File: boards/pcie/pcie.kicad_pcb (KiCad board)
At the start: 4 copper layers, 167.7 x 111.2 mm, 136 parts, among them J1 PCIexpress_bracket, J10 HDMI_A, J11 HDMI_A, J2 PCIexpress_x16, J3 12V, J4 5V, J5 3V3, J6 1V0, J7 GND, J8 HDMI_A, J9 HDMI_A, U1 AP63203WU, U2 UPD720202K8-701-BAA, U3 AP63205WU, U4 TLV75801PDBVR, U5 CH334F, U6 CH334F, U7 CH334F, U8 CH334F

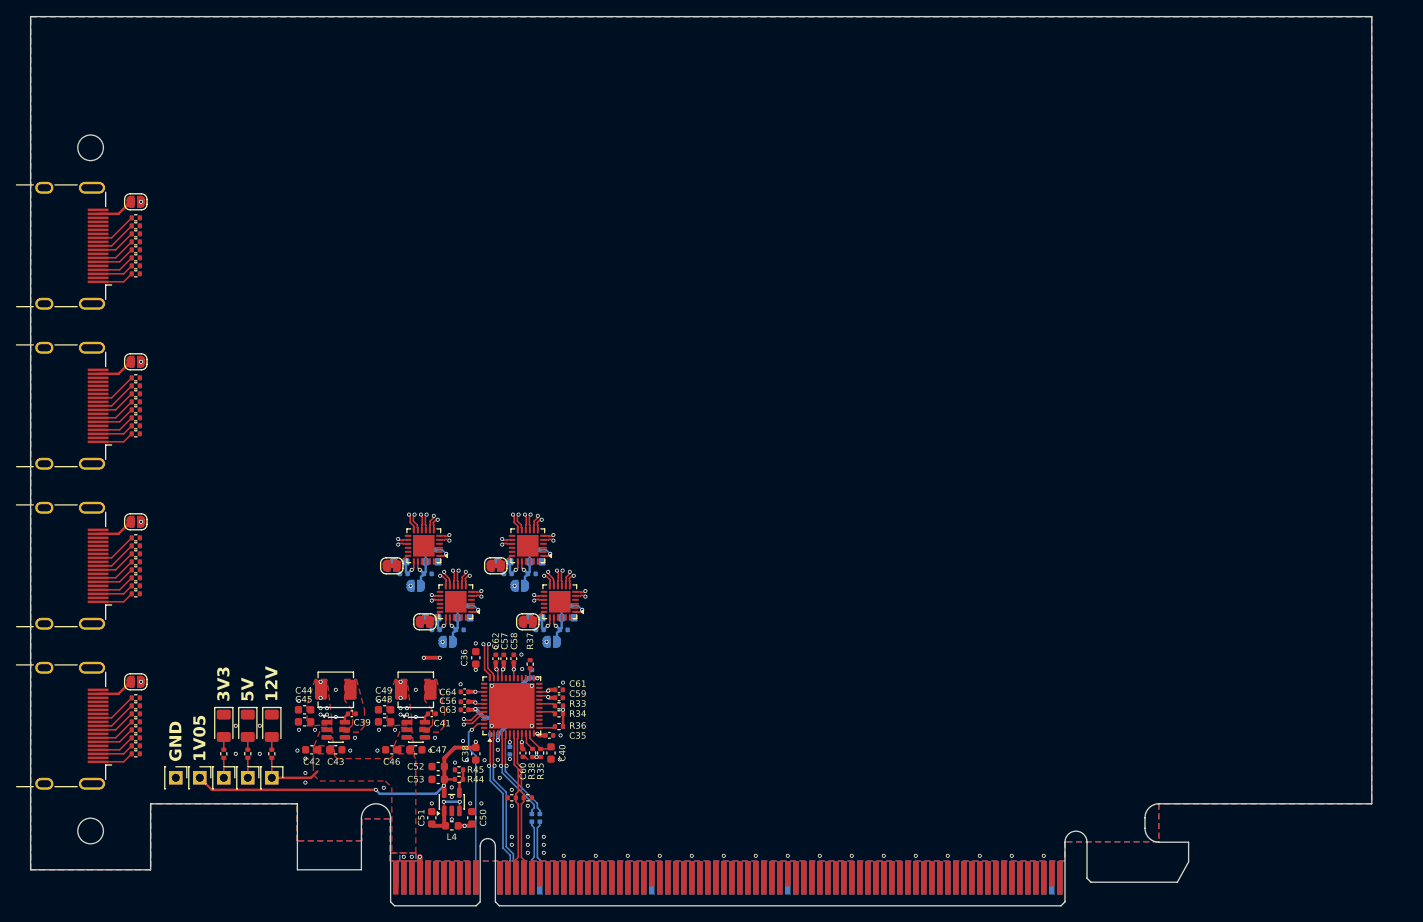
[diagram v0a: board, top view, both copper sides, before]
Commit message: pcie: add leds, buck regulators
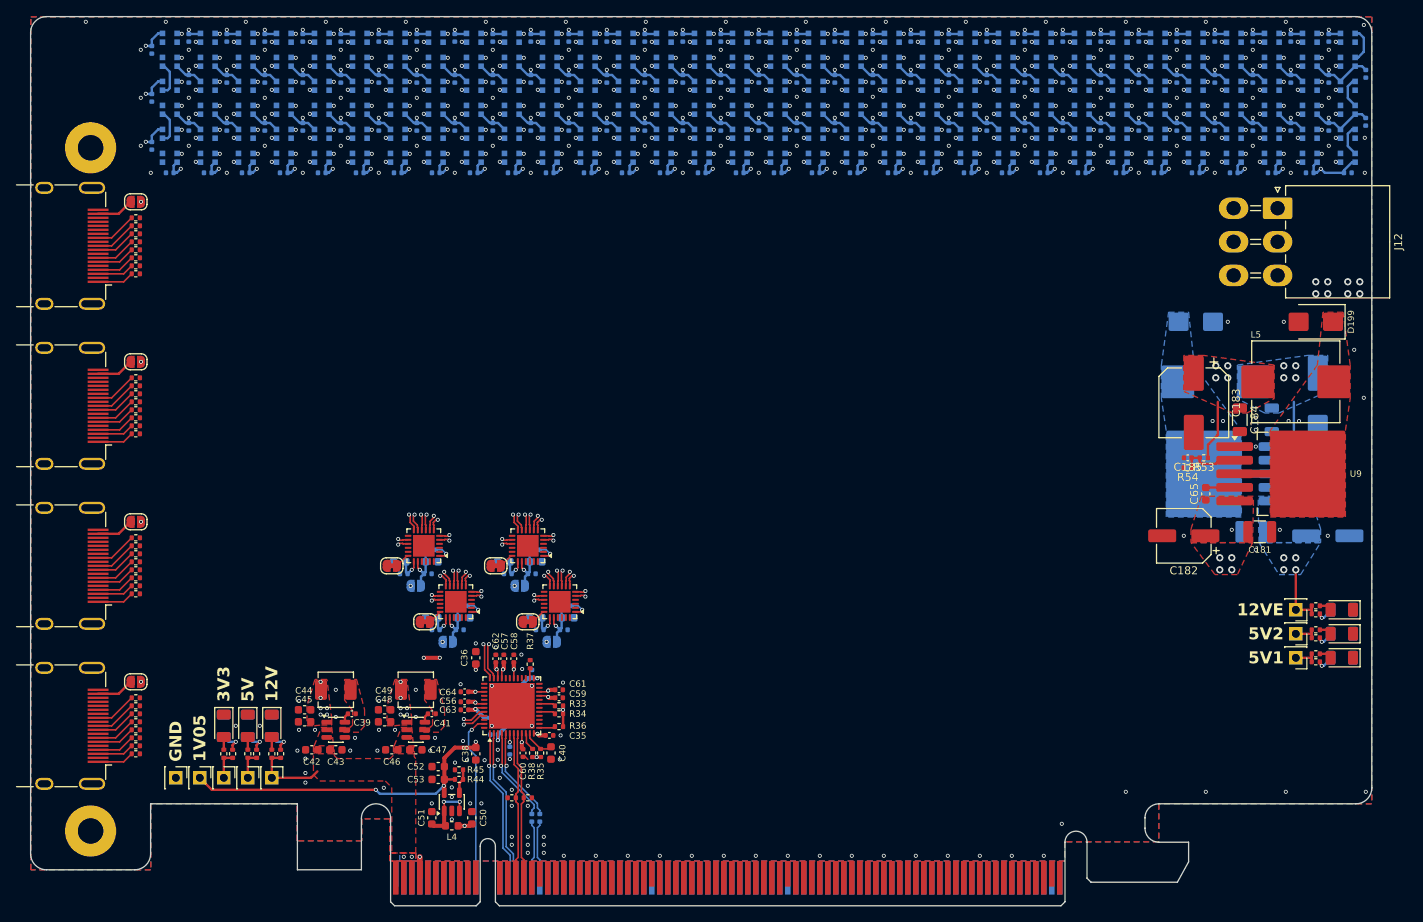
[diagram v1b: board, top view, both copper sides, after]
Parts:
- added C100: 100nF, Capacitor_SMD:C_0402_1005Metric, B.Cu at (165.0, 96.8)
- added C101: 100nF, Capacitor_SMD:C_0402_1005Metric, B.Cu at (174.5, 96.8)
- added C102: 100nF, Capacitor_SMD:C_0402_1005Metric, B.Cu at (169.8, 96.8)
- added C103: 100nF, Capacitor_SMD:C_0402_1005Metric, B.Cu at (179.2, 96.8)
- added C104: 100nF, Capacitor_SMD:C_0402_1005Metric, B.Cu at (207.8, 96.8)
- added C105: 100nF, Capacitor_SMD:C_0402_1005Metric, B.Cu at (203.0, 96.8)
- added C106: 100nF, Capacitor_SMD:C_0402_1005Metric, B.Cu at (198.2, 96.8)
- added C107: 100nF, Capacitor_SMD:C_0402_1005Metric, B.Cu at (193.5, 96.8)
- added C108: 100nF, Capacitor_SMD:C_0402_1005Metric, B.Cu at (184.0, 96.8)
- added C109: 100nF, Capacitor_SMD:C_0402_1005Metric, B.Cu at (188.8, 96.8)
- added C110: 100nF, Capacitor_SMD:C_0402_1005Metric, B.Cu at (136.5, 96.8)
- added C111: 100nF, Capacitor_SMD:C_0402_1005Metric, B.Cu at (141.2, 96.8)
- added C112: 100nF, Capacitor_SMD:C_0402_1005Metric, B.Cu at (224.4, 102.5)
- added C113: 100nF, Capacitor_SMD:C_0402_1005Metric, B.Cu at (212.5, 96.8)
- added C114: 100nF, Capacitor_SMD:C_0402_1005Metric, B.Cu at (217.2, 96.8)
- added C115: 100nF, Capacitor_SMD:C_0402_1005Metric, B.Cu at (222.0, 96.8)
- added C116: 100nF, Capacitor_SMD:C_0402_1005Metric, B.Cu at (226.8, 96.8)
- added C117: 100nF, Capacitor_SMD:C_0402_1005Metric, B.Cu at (96.1, 102.5)
- added C118: 100nF, Capacitor_SMD:C_0402_1005Metric, B.Cu at (134.1, 102.5)
- added C119: 100nF, Capacitor_SMD:C_0402_1005Metric, B.Cu at (153.1, 102.5)
- added C120: 100nF, Capacitor_SMD:C_0402_1005Metric, B.Cu at (115.1, 102.5)
- added C121: 100nF, Capacitor_SMD:C_0402_1005Metric, B.Cu at (172.1, 102.5)
- added C122: 100nF, Capacitor_SMD:C_0402_1005Metric, B.Cu at (219.6, 102.5)
- added C123: 100nF, Capacitor_SMD:C_0402_1005Metric, B.Cu at (200.6, 102.5)
- added C124: 100nF, Capacitor_SMD:C_0402_1005Metric, B.Cu at (191.1, 102.5)
- added C125: 100nF, Capacitor_SMD:C_0402_1005Metric, B.Cu at (91.4, 102.5)
- added C126: 100nF, Capacitor_SMD:C_0402_1005Metric, B.Cu at (129.4, 102.5)
- added C127: 100nF, Capacitor_SMD:C_0402_1005Metric, B.Cu at (148.4, 102.5)
- added C128: 100nF, Capacitor_SMD:C_0402_1005Metric, B.Cu at (110.4, 102.5)
- added C129: 100nF, Capacitor_SMD:C_0402_1005Metric, B.Cu at (167.4, 102.5)
- added C130: 100nF, Capacitor_SMD:C_0402_1005Metric, B.Cu at (214.9, 102.5)
- added C131: 100nF, Capacitor_SMD:C_0402_1005Metric, B.Cu at (195.9, 102.5)
- added C132: 100nF, Capacitor_SMD:C_0402_1005Metric, B.Cu at (229.1, 102.5)
- added C133: 100nF, Capacitor_SMD:C_0402_1005Metric, B.Cu at (86.6, 102.5)
- added C134: 100nF, Capacitor_SMD:C_0402_1005Metric, B.Cu at (124.6, 102.5)
- added C135: 100nF, Capacitor_SMD:C_0402_1005Metric, B.Cu at (143.6, 102.5)
- added C136: 100nF, Capacitor_SMD:C_0402_1005Metric, B.Cu at (105.6, 102.5)
- added C137: 100nF, Capacitor_SMD:C_0402_1005Metric, B.Cu at (162.6, 102.5)
- added C138: 100nF, Capacitor_SMD:C_0402_1005Metric, B.Cu at (210.1, 102.5)
- added C139: 100nF, Capacitor_SMD:C_0402_1005Metric, B.Cu at (186.4, 102.5)
- added C140: 100nF, Capacitor_SMD:C_0402_1005Metric, B.Cu at (176.9, 102.5)
- added C141: 100nF, Capacitor_SMD:C_0402_1005Metric, B.Cu at (81.9, 102.5)
- added C142: 100nF, Capacitor_SMD:C_0402_1005Metric, B.Cu at (119.9, 102.5)
- added C143: 100nF, Capacitor_SMD:C_0402_1005Metric, B.Cu at (138.9, 102.5)
- added C144: 100nF, Capacitor_SMD:C_0402_1005Metric, B.Cu at (100.9, 102.5)
- added C145: 100nF, Capacitor_SMD:C_0402_1005Metric, B.Cu at (157.9, 102.5)
- added C146: 100nF, Capacitor_SMD:C_0402_1005Metric, B.Cu at (205.4, 102.5)
- added C147: 100nF, Capacitor_SMD:C_0402_1005Metric, B.Cu at (181.6, 102.5)
- added C148: 100nF, Capacitor_SMD:C_0402_1005Metric, B.Cu at (231.4, 96.1)
- added C149: 100nF, Capacitor_SMD:C_0402_1005Metric, B.Cu at (184.0, 85.6)
- added C150: 100nF, Capacitor_SMD:C_0402_1005Metric, B.Cu at (188.8, 85.6)
- added C151: 100nF, Capacitor_SMD:C_0402_1005Metric, B.Cu at (193.5, 85.6)
- added C152: 100nF, Capacitor_SMD:C_0402_1005Metric, B.Cu at (198.2, 85.6)
- added C153: 100nF, Capacitor_SMD:C_0402_1005Metric, B.Cu at (203.0, 85.6)
- added C154: 100nF, Capacitor_SMD:C_0402_1005Metric, B.Cu at (207.8, 85.6)
- added C155: 100nF, Capacitor_SMD:C_0402_1005Metric, B.Cu at (212.5, 85.6)
- added C156: 100nF, Capacitor_SMD:C_0402_1005Metric, B.Cu at (217.2, 85.6)
- added C157: 100nF, Capacitor_SMD:C_0402_1005Metric, B.Cu at (146.0, 85.6)
- added C158: 100nF, Capacitor_SMD:C_0402_1005Metric, B.Cu at (150.8, 85.6)
- added C159: 100nF, Capacitor_SMD:C_0402_1005Metric, B.Cu at (155.5, 85.6)
- added C160: 100nF, Capacitor_SMD:C_0402_1005Metric, B.Cu at (160.2, 85.6)
- added C161: 100nF, Capacitor_SMD:C_0402_1005Metric, B.Cu at (165.0, 85.6)
- added C162: 100nF, Capacitor_SMD:C_0402_1005Metric, B.Cu at (169.8, 85.6)
- added C163: 100nF, Capacitor_SMD:C_0402_1005Metric, B.Cu at (174.5, 85.6)
- added C164: 100nF, Capacitor_SMD:C_0402_1005Metric, B.Cu at (179.2, 85.6)
- added C165: 100nF, Capacitor_SMD:C_0402_1005Metric, B.Cu at (108.0, 85.6)
- added C166: 100nF, Capacitor_SMD:C_0402_1005Metric, B.Cu at (112.8, 85.6)
- added C167: 100nF, Capacitor_SMD:C_0402_1005Metric, B.Cu at (117.5, 85.6)
- added C168: 100nF, Capacitor_SMD:C_0402_1005Metric, B.Cu at (122.2, 85.6)
- added C169: 100nF, Capacitor_SMD:C_0402_1005Metric, B.Cu at (127.0, 85.6)
- added C170: 100nF, Capacitor_SMD:C_0402_1005Metric, B.Cu at (131.8, 85.6)
- added C171: 100nF, Capacitor_SMD:C_0402_1005Metric, B.Cu at (136.5, 85.6)
- added C172: 100nF, Capacitor_SMD:C_0402_1005Metric, B.Cu at (141.2, 85.6)
- added C173: 100nF, Capacitor_SMD:C_0402_1005Metric, B.Cu at (84.2, 85.6)
- added C174: 100nF, Capacitor_SMD:C_0402_1005Metric, B.Cu at (89.0, 85.6)
- added C175: 100nF, Capacitor_SMD:C_0402_1005Metric, B.Cu at (93.8, 85.6)
- added C176: 100nF, Capacitor_SMD:C_0402_1005Metric, B.Cu at (98.5, 85.6)
- added C177: 100nF, Capacitor_SMD:C_0402_1005Metric, B.Cu at (103.2, 85.6)
- added C178: 100nF, Capacitor_SMD:C_0402_1005Metric, B.Cu at (231.4, 90.1)
- added C179: 100nF, Capacitor_SMD:C_0402_1005Metric, B.Cu at (226.8, 85.6)
- added C180: 100nF, Capacitor_SMD:C_0402_1005Metric, B.Cu at (222.0, 85.6)
- added C181: 22uF@25V, Capacitor_SMD:C_1210_3225Metric, F.Cu at (218.1, 147.4)
- added C182: 220uF@25V, Capacitor_SMD:CP_Elec_6.3x7.7, F.Cu at (208.6, 147.9)
- added C183: 470uF@16V, Capacitor_SMD:CP_Elec_8x10.5, F.Cu at (209.9, 131.2)
- added C184: 22uF@10V, Capacitor_SMD:C_1206_3216Metric, F.Cu at (215.6, 133.4)
- added C185: 33nF, Capacitor_SMD:C_0402_1005Metric, F.Cu at (209.1, 138.1)
- added C186: 220uF@25V, Capacitor_SMD:CP_Elec_6.3x7.7, B.Cu at (226.6, 147.9)
- added C187: 22uF@25V, Capacitor_SMD:C_1210_3225Metric, B.Cu at (217.1, 147.4)
- added C188: 1uF, Capacitor_SMD:C_0603_1608Metric, B.Cu at (223.9, 142.6)
- added C189: 33nF, Capacitor_SMD:C_0402_1005Metric, B.Cu at (226.1, 138.1)
- added C19: 100nF, Capacitor_SMD:C_0402_1005Metric, B.Cu at (79.6, 87.1)
- added C190: 22uF@10V, Capacitor_SMD:C_1206_3216Metric, B.Cu at (219.6, 133.4)
- added C191: 470uF@16V, Capacitor_SMD:CP_Elec_8x10.5, B.Cu at (225.4, 131.2)
- added C20: 100nF, Capacitor_SMD:C_0402_1005Metric, B.Cu at (79.6, 93.1)
- added C21: 100nF, Capacitor_SMD:C_0402_1005Metric, B.Cu at (89.0, 90.8)
- added C22: 100nF, Capacitor_SMD:C_0402_1005Metric, B.Cu at (84.2, 90.8)
- added C23: 100nF, Capacitor_SMD:C_0402_1005Metric, B.Cu at (93.8, 96.8)
- added C24: 100nF, Capacitor_SMD:C_0402_1005Metric, B.Cu at (89.0, 96.8)
- added C25: 100nF, Capacitor_SMD:C_0402_1005Metric, B.Cu at (84.2, 96.8)
- added C26: 100nF, Capacitor_SMD:C_0402_1005Metric, B.Cu at (79.6, 99.1)
- added C27: 100nF, Capacitor_SMD:C_0402_1005Metric, B.Cu at (93.8, 90.8)
- added C28: 100nF, Capacitor_SMD:C_0402_1005Metric, B.Cu at (98.5, 90.8)
- added C29: 100nF, Capacitor_SMD:C_0402_1005Metric, B.Cu at (103.2, 90.8)
- added C30: 100nF, Capacitor_SMD:C_0402_1005Metric, B.Cu at (108.0, 90.8)
- added C31: 100nF, Capacitor_SMD:C_0402_1005Metric, B.Cu at (112.8, 90.8)
- added C32: 100nF, Capacitor_SMD:C_0402_1005Metric, B.Cu at (117.5, 90.8)
- added C37: 100nF, Capacitor_SMD:C_0402_1005Metric, B.Cu at (122.2, 90.8)
- added C65: 1uF, Capacitor_SMD:C_0603_1608Metric, F.Cu at (211.4, 142.6)
- added C66: 100nF, Capacitor_SMD:C_0402_1005Metric, B.Cu at (127.0, 90.8)
- added C67: 100nF, Capacitor_SMD:C_0402_1005Metric, B.Cu at (131.8, 90.8)
- added C68: 100nF, Capacitor_SMD:C_0402_1005Metric, B.Cu at (174.5, 90.8)
- added C69: 100nF, Capacitor_SMD:C_0402_1005Metric, B.Cu at (179.2, 90.8)
- added C70: 100nF, Capacitor_SMD:C_0402_1005Metric, B.Cu at (184.0, 90.8)
- added C71: 100nF, Capacitor_SMD:C_0402_1005Metric, B.Cu at (188.8, 90.8)
- added C72: 100nF, Capacitor_SMD:C_0402_1005Metric, B.Cu at (155.5, 90.8)
- added C73: 100nF, Capacitor_SMD:C_0402_1005Metric, B.Cu at (160.2, 90.8)
- added C74: 100nF, Capacitor_SMD:C_0402_1005Metric, B.Cu at (165.0, 90.8)
- added C75: 100nF, Capacitor_SMD:C_0402_1005Metric, B.Cu at (169.8, 90.8)
- added C76: 100nF, Capacitor_SMD:C_0402_1005Metric, B.Cu at (141.2, 90.8)
- added C77: 100nF, Capacitor_SMD:C_0402_1005Metric, B.Cu at (136.5, 90.8)
- added C78: 100nF, Capacitor_SMD:C_0402_1005Metric, B.Cu at (150.8, 90.8)
- added C79: 100nF, Capacitor_SMD:C_0402_1005Metric, B.Cu at (146.0, 90.8)
- added C80: 100nF, Capacitor_SMD:C_0402_1005Metric, B.Cu at (193.5, 90.8)
- added C81: 100nF, Capacitor_SMD:C_0402_1005Metric, B.Cu at (198.2, 90.8)
- added C82: 100nF, Capacitor_SMD:C_0402_1005Metric, B.Cu at (203.0, 90.8)
- added C83: 100nF, Capacitor_SMD:C_0402_1005Metric, B.Cu at (207.8, 90.8)
- added C84: 100nF, Capacitor_SMD:C_0402_1005Metric, B.Cu at (226.8, 90.8)
- added C85: 100nF, Capacitor_SMD:C_0402_1005Metric, B.Cu at (212.5, 90.8)
- added C86: 100nF, Capacitor_SMD:C_0402_1005Metric, B.Cu at (217.2, 90.8)
- added C87: 100nF, Capacitor_SMD:C_0402_1005Metric, B.Cu at (222.0, 90.8)
- added C88: 100nF, Capacitor_SMD:C_0402_1005Metric, B.Cu at (98.5, 96.8)
- added C89: 100nF, Capacitor_SMD:C_0402_1005Metric, B.Cu at (103.2, 96.8)
- added C90: 100nF, Capacitor_SMD:C_0402_1005Metric, B.Cu at (112.8, 96.8)
- added C91: 100nF, Capacitor_SMD:C_0402_1005Metric, B.Cu at (108.0, 96.8)
- added C92: 100nF, Capacitor_SMD:C_0402_1005Metric, B.Cu at (117.5, 96.8)
- added C93: 100nF, Capacitor_SMD:C_0402_1005Metric, B.Cu at (122.2, 96.8)
- added C94: 100nF, Capacitor_SMD:C_0402_1005Metric, B.Cu at (127.0, 96.8)
- added C95: 100nF, Capacitor_SMD:C_0402_1005Metric, B.Cu at (131.8, 96.8)
- added C96: 100nF, Capacitor_SMD:C_0402_1005Metric, B.Cu at (150.8, 96.8)
- added C97: 100nF, Capacitor_SMD:C_0402_1005Metric, B.Cu at (155.5, 96.8)
- added C98: 100nF, Capacitor_SMD:C_0402_1005Metric, B.Cu at (146.0, 96.8)
- added C99: 100nF, Capacitor_SMD:C_0402_1005Metric, B.Cu at (160.2, 96.8)
- added D10: LED_45deg, pcie:LED_WS2812B-2020_PLCC4_2.0x2.0mm, B.Cu at (96.1, 85.6)
- added D100: LED_45deg, pcie:LED_WS2812B-2020_PLCC4_2.0x2.0mm, B.Cu at (219.6, 91.6)
- added D101: LED_45deg, pcie:LED_WS2812B-2020_PLCC4_2.0x2.0mm, B.Cu at (224.4, 91.6)
- added D102: LED_45deg, pcie:LED_WS2812B-2020_PLCC4_2.0x2.0mm, B.Cu at (229.1, 91.6)
- added D103: LED_45deg, pcie:LED_WS2812B-2020_PLCC4_2.0x2.0mm, B.Cu at (229.1, 94.6)
- added D104: LED_45deg, pcie:LED_WS2812B-2020_PLCC4_2.0x2.0mm, B.Cu at (224.4, 94.6)
- added D105: LED_45deg, pcie:LED_WS2812B-2020_PLCC4_2.0x2.0mm, B.Cu at (219.6, 94.6)
- added D106: LED_45deg, pcie:LED_WS2812B-2020_PLCC4_2.0x2.0mm, B.Cu at (214.9, 94.6)
- added D107: LED_45deg, pcie:LED_WS2812B-2020_PLCC4_2.0x2.0mm, B.Cu at (210.1, 94.6)
- added D108: LED_45deg, pcie:LED_WS2812B-2020_PLCC4_2.0x2.0mm, B.Cu at (205.4, 94.6)
- added D109: LED_45deg, pcie:LED_WS2812B-2020_PLCC4_2.0x2.0mm, B.Cu at (200.6, 94.6)
- added D11: LED_45deg, pcie:LED_WS2812B-2020_PLCC4_2.0x2.0mm, B.Cu at (100.9, 85.6)
- added D110: LED_45deg, pcie:LED_WS2812B-2020_PLCC4_2.0x2.0mm, B.Cu at (195.9, 94.6)
- added D111: LED_45deg, pcie:LED_WS2812B-2020_PLCC4_2.0x2.0mm, B.Cu at (191.1, 94.6)
- added D112: LED_45deg, pcie:LED_WS2812B-2020_PLCC4_2.0x2.0mm, B.Cu at (186.4, 94.6)
- added D113: LED_45deg, pcie:LED_WS2812B-2020_PLCC4_2.0x2.0mm, B.Cu at (181.6, 94.6)
- added D114: LED_45deg, pcie:LED_WS2812B-2020_PLCC4_2.0x2.0mm, B.Cu at (176.9, 94.6)
- added D115: LED_45deg, pcie:LED_WS2812B-2020_PLCC4_2.0x2.0mm, B.Cu at (172.1, 94.6)
- added D116: LED_45deg, pcie:LED_WS2812B-2020_PLCC4_2.0x2.0mm, B.Cu at (167.4, 94.6)
- added D117: LED_45deg, pcie:LED_WS2812B-2020_PLCC4_2.0x2.0mm, B.Cu at (162.6, 94.6)
- added D118: LED_45deg, pcie:LED_WS2812B-2020_PLCC4_2.0x2.0mm, B.Cu at (157.9, 94.6)
- added D119: LED_45deg, pcie:LED_WS2812B-2020_PLCC4_2.0x2.0mm, B.Cu at (153.1, 94.6)
- added D12: LED_45deg, pcie:LED_WS2812B-2020_PLCC4_2.0x2.0mm, B.Cu at (105.6, 85.6)
- added D120: LED_45deg, pcie:LED_WS2812B-2020_PLCC4_2.0x2.0mm, B.Cu at (148.4, 94.6)
- added D121: LED_45deg, pcie:LED_WS2812B-2020_PLCC4_2.0x2.0mm, B.Cu at (143.6, 94.6)
- added D122: LED_45deg, pcie:LED_WS2812B-2020_PLCC4_2.0x2.0mm, B.Cu at (138.9, 94.6)
- added D123: LED_45deg, pcie:LED_WS2812B-2020_PLCC4_2.0x2.0mm, B.Cu at (134.1, 94.6)
- added D124: LED_45deg, pcie:LED_WS2812B-2020_PLCC4_2.0x2.0mm, B.Cu at (129.4, 94.6)
- added D125: LED_45deg, pcie:LED_WS2812B-2020_PLCC4_2.0x2.0mm, B.Cu at (124.6, 94.6)
- added D126: LED_45deg, pcie:LED_WS2812B-2020_PLCC4_2.0x2.0mm, B.Cu at (119.9, 94.6)
- added D127: LED_45deg, pcie:LED_WS2812B-2020_PLCC4_2.0x2.0mm, B.Cu at (115.1, 94.6)
- added D128: LED_45deg, pcie:LED_WS2812B-2020_PLCC4_2.0x2.0mm, B.Cu at (110.4, 94.6)
- added D129: LED_45deg, pcie:LED_WS2812B-2020_PLCC4_2.0x2.0mm, B.Cu at (105.6, 94.6)
- added D13: LED_45deg, pcie:LED_WS2812B-2020_PLCC4_2.0x2.0mm, B.Cu at (110.4, 85.6)
- added D130: LED_45deg, pcie:LED_WS2812B-2020_PLCC4_2.0x2.0mm, B.Cu at (100.9, 94.6)
- added D131: LED_45deg, pcie:LED_WS2812B-2020_PLCC4_2.0x2.0mm, B.Cu at (96.1, 94.6)
- added D132: LED_45deg, pcie:LED_WS2812B-2020_PLCC4_2.0x2.0mm, B.Cu at (91.4, 94.6)
- added D133: LED_45deg, pcie:LED_WS2812B-2020_PLCC4_2.0x2.0mm, B.Cu at (86.6, 94.6)
- added D134: LED_45deg, pcie:LED_WS2812B-2020_PLCC4_2.0x2.0mm, B.Cu at (81.9, 94.6)
- added D135: LED_45deg, pcie:LED_WS2812B-2020_PLCC4_2.0x2.0mm, B.Cu at (81.9, 97.6)
- added D136: LED_45deg, pcie:LED_WS2812B-2020_PLCC4_2.0x2.0mm, B.Cu at (86.6, 97.6)
- added D137: LED_45deg, pcie:LED_WS2812B-2020_PLCC4_2.0x2.0mm, B.Cu at (91.4, 97.6)
- added D138: LED_45deg, pcie:LED_WS2812B-2020_PLCC4_2.0x2.0mm, B.Cu at (96.1, 97.6)
- added D139: LED_45deg, pcie:LED_WS2812B-2020_PLCC4_2.0x2.0mm, B.Cu at (100.9, 97.6)
- added D14: LED_45deg, pcie:LED_WS2812B-2020_PLCC4_2.0x2.0mm, B.Cu at (115.1, 85.6)
- added D140: LED_45deg, pcie:LED_WS2812B-2020_PLCC4_2.0x2.0mm, B.Cu at (105.6, 97.6)
- added D141: LED_45deg, pcie:LED_WS2812B-2020_PLCC4_2.0x2.0mm, B.Cu at (110.4, 97.6)
- added D142: LED_45deg, pcie:LED_WS2812B-2020_PLCC4_2.0x2.0mm, B.Cu at (115.1, 97.6)
- added D143: LED_45deg, pcie:LED_WS2812B-2020_PLCC4_2.0x2.0mm, B.Cu at (119.9, 97.6)
- added D144: LED_45deg, pcie:LED_WS2812B-2020_PLCC4_2.0x2.0mm, B.Cu at (124.6, 97.6)
- added D145: LED_45deg, pcie:LED_WS2812B-2020_PLCC4_2.0x2.0mm, B.Cu at (129.4, 97.6)
- added D146: LED_45deg, pcie:LED_WS2812B-2020_PLCC4_2.0x2.0mm, B.Cu at (134.1, 97.6)
- added D147: LED_45deg, pcie:LED_WS2812B-2020_PLCC4_2.0x2.0mm, B.Cu at (138.9, 97.6)
- added D148: LED_45deg, pcie:LED_WS2812B-2020_PLCC4_2.0x2.0mm, B.Cu at (143.6, 97.6)
- added D149: LED_45deg, pcie:LED_WS2812B-2020_PLCC4_2.0x2.0mm, B.Cu at (148.4, 97.6)
- added D15: LED_45deg, pcie:LED_WS2812B-2020_PLCC4_2.0x2.0mm, B.Cu at (119.9, 85.6)
- added D150: LED_45deg, pcie:LED_WS2812B-2020_PLCC4_2.0x2.0mm, B.Cu at (153.1, 97.6)
- added D151: LED_45deg, pcie:LED_WS2812B-2020_PLCC4_2.0x2.0mm, B.Cu at (157.9, 97.6)
- added D152: LED_45deg, pcie:LED_WS2812B-2020_PLCC4_2.0x2.0mm, B.Cu at (162.6, 97.6)
- added D153: LED_45deg, pcie:LED_WS2812B-2020_PLCC4_2.0x2.0mm, B.Cu at (167.4, 97.6)
- added D154: LED_45deg, pcie:LED_WS2812B-2020_PLCC4_2.0x2.0mm, B.Cu at (172.1, 97.6)
- added D155: LED_45deg, pcie:LED_WS2812B-2020_PLCC4_2.0x2.0mm, B.Cu at (176.9, 97.6)
- added D156: LED_45deg, pcie:LED_WS2812B-2020_PLCC4_2.0x2.0mm, B.Cu at (181.6, 97.6)
- added D157: LED_45deg, pcie:LED_WS2812B-2020_PLCC4_2.0x2.0mm, B.Cu at (186.4, 97.6)
- added D158: LED_45deg, pcie:LED_WS2812B-2020_PLCC4_2.0x2.0mm, B.Cu at (191.1, 97.6)
- added D159: LED_45deg, pcie:LED_WS2812B-2020_PLCC4_2.0x2.0mm, B.Cu at (195.9, 97.6)
- added D16: LED_45deg, pcie:LED_WS2812B-2020_PLCC4_2.0x2.0mm, B.Cu at (124.6, 85.6)
- added D160: LED_45deg, pcie:LED_WS2812B-2020_PLCC4_2.0x2.0mm, B.Cu at (200.6, 97.6)
- added D161: LED_45deg, pcie:LED_WS2812B-2020_PLCC4_2.0x2.0mm, B.Cu at (205.4, 97.6)
- added D162: LED_45deg, pcie:LED_WS2812B-2020_PLCC4_2.0x2.0mm, B.Cu at (210.1, 97.6)
- added D163: LED_45deg, pcie:LED_WS2812B-2020_PLCC4_2.0x2.0mm, B.Cu at (214.9, 97.6)
- added D164: LED_45deg, pcie:LED_WS2812B-2020_PLCC4_2.0x2.0mm, B.Cu at (219.6, 97.6)
- added D165: LED_45deg, pcie:LED_WS2812B-2020_PLCC4_2.0x2.0mm, B.Cu at (224.4, 97.6)
- added D166: LED_45deg, pcie:LED_WS2812B-2020_PLCC4_2.0x2.0mm, B.Cu at (229.1, 97.6)
- added D167: LED_45deg, pcie:LED_WS2812B-2020_PLCC4_2.0x2.0mm, B.Cu at (229.1, 100.6)
- added D168: LED_45deg, pcie:LED_WS2812B-2020_PLCC4_2.0x2.0mm, B.Cu at (224.4, 100.6)
- added D169: LED_45deg, pcie:LED_WS2812B-2020_PLCC4_2.0x2.0mm, B.Cu at (219.6, 100.6)
- added D17: LED_45deg, pcie:LED_WS2812B-2020_PLCC4_2.0x2.0mm, B.Cu at (129.4, 85.6)
- added D170: LED_45deg, pcie:LED_WS2812B-2020_PLCC4_2.0x2.0mm, B.Cu at (214.9, 100.6)
- added D171: LED_45deg, pcie:LED_WS2812B-2020_PLCC4_2.0x2.0mm, B.Cu at (210.1, 100.6)
- added D172: LED_45deg, pcie:LED_WS2812B-2020_PLCC4_2.0x2.0mm, B.Cu at (205.4, 100.6)
- added D173: LED_45deg, pcie:LED_WS2812B-2020_PLCC4_2.0x2.0mm, B.Cu at (200.6, 100.6)
- added D174: LED_45deg, pcie:LED_WS2812B-2020_PLCC4_2.0x2.0mm, B.Cu at (195.9, 100.6)
- added D175: LED_45deg, pcie:LED_WS2812B-2020_PLCC4_2.0x2.0mm, B.Cu at (191.1, 100.6)
- added D176: LED_45deg, pcie:LED_WS2812B-2020_PLCC4_2.0x2.0mm, B.Cu at (186.4, 100.6)
- added D177: LED_45deg, pcie:LED_WS2812B-2020_PLCC4_2.0x2.0mm, B.Cu at (181.6, 100.6)
- added D178: LED_45deg, pcie:LED_WS2812B-2020_PLCC4_2.0x2.0mm, B.Cu at (176.9, 100.6)
- added D179: LED_45deg, pcie:LED_WS2812B-2020_PLCC4_2.0x2.0mm, B.Cu at (172.1, 100.6)
- added D18: LED_45deg, pcie:LED_WS2812B-2020_PLCC4_2.0x2.0mm, B.Cu at (134.1, 85.6)
- added D180: LED_45deg, pcie:LED_WS2812B-2020_PLCC4_2.0x2.0mm, B.Cu at (167.4, 100.6)
- added D181: LED_45deg, pcie:LED_WS2812B-2020_PLCC4_2.0x2.0mm, B.Cu at (162.6, 100.6)
- added D182: LED_45deg, pcie:LED_WS2812B-2020_PLCC4_2.0x2.0mm, B.Cu at (157.9, 100.6)
- added D183: LED_45deg, pcie:LED_WS2812B-2020_PLCC4_2.0x2.0mm, B.Cu at (153.1, 100.6)
- added D184: LED_45deg, pcie:LED_WS2812B-2020_PLCC4_2.0x2.0mm, B.Cu at (148.4, 100.6)
- added D185: LED_45deg, pcie:LED_WS2812B-2020_PLCC4_2.0x2.0mm, B.Cu at (143.6, 100.6)
- added D186: LED_45deg, pcie:LED_WS2812B-2020_PLCC4_2.0x2.0mm, B.Cu at (138.9, 100.6)
- added D187: LED_45deg, pcie:LED_WS2812B-2020_PLCC4_2.0x2.0mm, B.Cu at (134.1, 100.6)
- added D188: LED_45deg, pcie:LED_WS2812B-2020_PLCC4_2.0x2.0mm, B.Cu at (129.4, 100.6)
- added D189: LED_45deg, pcie:LED_WS2812B-2020_PLCC4_2.0x2.0mm, B.Cu at (124.6, 100.6)
- added D19: LED_45deg, pcie:LED_WS2812B-2020_PLCC4_2.0x2.0mm, B.Cu at (138.9, 85.6)
- added D190: LED_45deg, pcie:LED_WS2812B-2020_PLCC4_2.0x2.0mm, B.Cu at (119.9, 100.6)
- added D191: LED_45deg, pcie:LED_WS2812B-2020_PLCC4_2.0x2.0mm, B.Cu at (115.1, 100.6)
- added D192: LED_45deg, pcie:LED_WS2812B-2020_PLCC4_2.0x2.0mm, B.Cu at (110.4, 100.6)
- added D193: LED_45deg, pcie:LED_WS2812B-2020_PLCC4_2.0x2.0mm, B.Cu at (105.6, 100.6)
- added D194: LED_45deg, pcie:LED_WS2812B-2020_PLCC4_2.0x2.0mm, B.Cu at (100.9, 100.6)
- added D195: LED_45deg, pcie:LED_WS2812B-2020_PLCC4_2.0x2.0mm, B.Cu at (96.1, 100.6)
- added D196: LED_45deg, pcie:LED_WS2812B-2020_PLCC4_2.0x2.0mm, B.Cu at (91.4, 100.6)
- added D197: LED_45deg, pcie:LED_WS2812B-2020_PLCC4_2.0x2.0mm, B.Cu at (86.6, 100.6)
- added D198: LED_45deg, pcie:LED_WS2812B-2020_PLCC4_2.0x2.0mm, B.Cu at (81.9, 100.6)
- added D199: SS1045-SMB, Diode_SMD:D_SMB, F.Cu at (225.1, 121.1)
- added D20: LED_45deg, pcie:LED_WS2812B-2020_PLCC4_2.0x2.0mm, B.Cu at (143.6, 85.6)
- added D200: SS1045-SMB, Diode_SMD:D_SMB, B.Cu at (210.1, 121.1)
- added D201: 12VE, LED_SMD:LED_1206_3216Metric, F.Cu at (228.4, 157.1)
- added D202: 12VE, LED_SMD:LED_1206_3216Metric, B.Cu at (228.4, 157.1)
- added D203: LED_5V1, LED_SMD:LED_1206_3216Metric, F.Cu at (228.4, 163.1)
- added D204: LED_5V1, LED_SMD:LED_1206_3216Metric, B.Cu at (228.4, 163.1)
- added D205: LED_5V2, LED_SMD:LED_1206_3216Metric, F.Cu at (228.4, 160.1)
- added D206: LED_5V2, LED_SMD:LED_1206_3216Metric, B.Cu at (228.4, 160.1)
- added D21: LED_45deg, pcie:LED_WS2812B-2020_PLCC4_2.0x2.0mm, B.Cu at (148.4, 85.6)
- added D22: LED_45deg, pcie:LED_WS2812B-2020_PLCC4_2.0x2.0mm, B.Cu at (153.1, 85.6)
- added D23: LED_45deg, pcie:LED_WS2812B-2020_PLCC4_2.0x2.0mm, B.Cu at (157.9, 85.6)
- added D24: LED_45deg, pcie:LED_WS2812B-2020_PLCC4_2.0x2.0mm, B.Cu at (162.6, 85.6)
- added D25: LED_45deg, pcie:LED_WS2812B-2020_PLCC4_2.0x2.0mm, B.Cu at (167.4, 85.6)
- added D26: LED_45deg, pcie:LED_WS2812B-2020_PLCC4_2.0x2.0mm, B.Cu at (172.1, 85.6)
- added D27: LED_45deg, pcie:LED_WS2812B-2020_PLCC4_2.0x2.0mm, B.Cu at (176.9, 85.6)
- added D28: LED_45deg, pcie:LED_WS2812B-2020_PLCC4_2.0x2.0mm, B.Cu at (181.6, 85.6)
- added D29: LED_45deg, pcie:LED_WS2812B-2020_PLCC4_2.0x2.0mm, B.Cu at (186.4, 85.6)
- added D30: LED_45deg, pcie:LED_WS2812B-2020_PLCC4_2.0x2.0mm, B.Cu at (191.1, 85.6)
- added D31: LED_45deg, pcie:LED_WS2812B-2020_PLCC4_2.0x2.0mm, B.Cu at (195.9, 85.6)
- added D32: LED_45deg, pcie:LED_WS2812B-2020_PLCC4_2.0x2.0mm, B.Cu at (200.6, 85.6)
- added D33: LED_45deg, pcie:LED_WS2812B-2020_PLCC4_2.0x2.0mm, B.Cu at (205.4, 85.6)
- added D34: LED_45deg, pcie:LED_WS2812B-2020_PLCC4_2.0x2.0mm, B.Cu at (210.1, 85.6)
- added D35: LED_45deg, pcie:LED_WS2812B-2020_PLCC4_2.0x2.0mm, B.Cu at (214.9, 85.6)
- added D36: LED_45deg, pcie:LED_WS2812B-2020_PLCC4_2.0x2.0mm, B.Cu at (219.6, 85.6)
- added D37: LED_45deg, pcie:LED_WS2812B-2020_PLCC4_2.0x2.0mm, B.Cu at (224.4, 85.6)
- added D38: LED_45deg, pcie:LED_WS2812B-2020_PLCC4_2.0x2.0mm, B.Cu at (229.1, 85.6)
- added D39: LED_45deg, pcie:LED_WS2812B-2020_PLCC4_2.0x2.0mm, B.Cu at (229.1, 88.6)
- added D4: 12V, LED_SMD:LED_1206_3216Metric, B.Cu at (94.6, 171.6)
- added D40: LED_45deg, pcie:LED_WS2812B-2020_PLCC4_2.0x2.0mm, B.Cu at (224.4, 88.6)
- added D41: LED_45deg, pcie:LED_WS2812B-2020_PLCC4_2.0x2.0mm, B.Cu at (219.6, 88.6)
- added D42: LED_45deg, pcie:LED_WS2812B-2020_PLCC4_2.0x2.0mm, B.Cu at (214.9, 88.6)
- added D43: LED_45deg, pcie:LED_WS2812B-2020_PLCC4_2.0x2.0mm, B.Cu at (210.1, 88.6)
- added D44: LED_45deg, pcie:LED_WS2812B-2020_PLCC4_2.0x2.0mm, B.Cu at (205.4, 88.6)
- added D45: LED_45deg, pcie:LED_WS2812B-2020_PLCC4_2.0x2.0mm, B.Cu at (200.6, 88.6)
- added D46: LED_45deg, pcie:LED_WS2812B-2020_PLCC4_2.0x2.0mm, B.Cu at (195.9, 88.6)
- added D47: LED_45deg, pcie:LED_WS2812B-2020_PLCC4_2.0x2.0mm, B.Cu at (191.1, 88.6)
- added D48: LED_45deg, pcie:LED_WS2812B-2020_PLCC4_2.0x2.0mm, B.Cu at (186.4, 88.6)
- added D49: LED_45deg, pcie:LED_WS2812B-2020_PLCC4_2.0x2.0mm, B.Cu at (181.6, 88.6)
- added D5: 5V, LED_SMD:LED_1206_3216Metric, B.Cu at (91.6, 171.6)
- added D50: LED_45deg, pcie:LED_WS2812B-2020_PLCC4_2.0x2.0mm, B.Cu at (176.9, 88.6)
- added D51: LED_45deg, pcie:LED_WS2812B-2020_PLCC4_2.0x2.0mm, B.Cu at (172.1, 88.6)
- added D52: LED_45deg, pcie:LED_WS2812B-2020_PLCC4_2.0x2.0mm, B.Cu at (167.4, 88.6)
- added D53: LED_45deg, pcie:LED_WS2812B-2020_PLCC4_2.0x2.0mm, B.Cu at (162.6, 88.6)
- added D54: LED_45deg, pcie:LED_WS2812B-2020_PLCC4_2.0x2.0mm, B.Cu at (157.9, 88.6)
- added D55: LED_45deg, pcie:LED_WS2812B-2020_PLCC4_2.0x2.0mm, B.Cu at (153.1, 88.6)
- added D56: LED_45deg, pcie:LED_WS2812B-2020_PLCC4_2.0x2.0mm, B.Cu at (148.4, 88.6)
- added D57: LED_45deg, pcie:LED_WS2812B-2020_PLCC4_2.0x2.0mm, B.Cu at (143.6, 88.6)
- added D58: LED_45deg, pcie:LED_WS2812B-2020_PLCC4_2.0x2.0mm, B.Cu at (138.9, 88.6)
- added D59: LED_45deg, pcie:LED_WS2812B-2020_PLCC4_2.0x2.0mm, B.Cu at (134.1, 88.6)
- added D6: 3V3, LED_SMD:LED_1206_3216Metric, B.Cu at (88.6, 171.6)
- added D60: LED_45deg, pcie:LED_WS2812B-2020_PLCC4_2.0x2.0mm, B.Cu at (129.4, 88.6)
- added D61: LED_45deg, pcie:LED_WS2812B-2020_PLCC4_2.0x2.0mm, B.Cu at (124.6, 88.6)
- added D62: LED_45deg, pcie:LED_WS2812B-2020_PLCC4_2.0x2.0mm, B.Cu at (119.9, 88.6)
- added D63: LED_45deg, pcie:LED_WS2812B-2020_PLCC4_2.0x2.0mm, B.Cu at (115.1, 88.6)
- added D64: LED_45deg, pcie:LED_WS2812B-2020_PLCC4_2.0x2.0mm, B.Cu at (110.4, 88.6)
- added D65: LED_45deg, pcie:LED_WS2812B-2020_PLCC4_2.0x2.0mm, B.Cu at (105.6, 88.6)
- added D66: LED_45deg, pcie:LED_WS2812B-2020_PLCC4_2.0x2.0mm, B.Cu at (100.9, 88.6)
- added D67: LED_45deg, pcie:LED_WS2812B-2020_PLCC4_2.0x2.0mm, B.Cu at (96.1, 88.6)
- added D68: LED_45deg, pcie:LED_WS2812B-2020_PLCC4_2.0x2.0mm, B.Cu at (91.4, 88.6)
- added D69: LED_45deg, pcie:LED_WS2812B-2020_PLCC4_2.0x2.0mm, B.Cu at (86.6, 88.6)
- added D7: LED_45deg, pcie:LED_WS2812B-2020_PLCC4_2.0x2.0mm, B.Cu at (81.9, 85.6)
- added D70: LED_45deg, pcie:LED_WS2812B-2020_PLCC4_2.0x2.0mm, B.Cu at (81.9, 88.6)
- added D71: LED_45deg, pcie:LED_WS2812B-2020_PLCC4_2.0x2.0mm, B.Cu at (81.9, 91.6)
- added D72: LED_45deg, pcie:LED_WS2812B-2020_PLCC4_2.0x2.0mm, B.Cu at (86.6, 91.6)
- added D73: LED_45deg, pcie:LED_WS2812B-2020_PLCC4_2.0x2.0mm, B.Cu at (91.4, 91.6)
- added D74: LED_45deg, pcie:LED_WS2812B-2020_PLCC4_2.0x2.0mm, B.Cu at (96.1, 91.6)
- added D75: LED_45deg, pcie:LED_WS2812B-2020_PLCC4_2.0x2.0mm, B.Cu at (100.9, 91.6)
- added D76: LED_45deg, pcie:LED_WS2812B-2020_PLCC4_2.0x2.0mm, B.Cu at (105.6, 91.6)
- added D77: LED_45deg, pcie:LED_WS2812B-2020_PLCC4_2.0x2.0mm, B.Cu at (110.4, 91.6)
- added D78: LED_45deg, pcie:LED_WS2812B-2020_PLCC4_2.0x2.0mm, B.Cu at (115.1, 91.6)
- added D79: LED_45deg, pcie:LED_WS2812B-2020_PLCC4_2.0x2.0mm, B.Cu at (119.9, 91.6)
- added D8: LED_45deg, pcie:LED_WS2812B-2020_PLCC4_2.0x2.0mm, B.Cu at (86.6, 85.6)
- added D80: LED_45deg, pcie:LED_WS2812B-2020_PLCC4_2.0x2.0mm, B.Cu at (124.6, 91.6)
- added D81: LED_45deg, pcie:LED_WS2812B-2020_PLCC4_2.0x2.0mm, B.Cu at (129.4, 91.6)
- added D82: LED_45deg, pcie:LED_WS2812B-2020_PLCC4_2.0x2.0mm, B.Cu at (134.1, 91.6)
- added D83: LED_45deg, pcie:LED_WS2812B-2020_PLCC4_2.0x2.0mm, B.Cu at (138.9, 91.6)
- added D84: LED_45deg, pcie:LED_WS2812B-2020_PLCC4_2.0x2.0mm, B.Cu at (143.6, 91.6)
- added D85: LED_45deg, pcie:LED_WS2812B-2020_PLCC4_2.0x2.0mm, B.Cu at (148.4, 91.6)
- added D86: LED_45deg, pcie:LED_WS2812B-2020_PLCC4_2.0x2.0mm, B.Cu at (153.1, 91.6)
- added D87: LED_45deg, pcie:LED_WS2812B-2020_PLCC4_2.0x2.0mm, B.Cu at (157.9, 91.6)
- added D88: LED_45deg, pcie:LED_WS2812B-2020_PLCC4_2.0x2.0mm, B.Cu at (162.6, 91.6)
- added D89: LED_45deg, pcie:LED_WS2812B-2020_PLCC4_2.0x2.0mm, B.Cu at (167.4, 91.6)
- added D9: LED_45deg, pcie:LED_WS2812B-2020_PLCC4_2.0x2.0mm, B.Cu at (91.4, 85.6)
- added D90: LED_45deg, pcie:LED_WS2812B-2020_PLCC4_2.0x2.0mm, B.Cu at (172.1, 91.6)
- added D91: LED_45deg, pcie:LED_WS2812B-2020_PLCC4_2.0x2.0mm, B.Cu at (176.9, 91.6)
- added D92: LED_45deg, pcie:LED_WS2812B-2020_PLCC4_2.0x2.0mm, B.Cu at (181.6, 91.6)
- added D93: LED_45deg, pcie:LED_WS2812B-2020_PLCC4_2.0x2.0mm, B.Cu at (186.4, 91.6)
- added D94: LED_45deg, pcie:LED_WS2812B-2020_PLCC4_2.0x2.0mm, B.Cu at (191.1, 91.6)
- added D95: LED_45deg, pcie:LED_WS2812B-2020_PLCC4_2.0x2.0mm, B.Cu at (195.9, 91.6)
- added D96: LED_45deg, pcie:LED_WS2812B-2020_PLCC4_2.0x2.0mm, B.Cu at (200.6, 91.6)
- added D97: LED_45deg, pcie:LED_WS2812B-2020_PLCC4_2.0x2.0mm, B.Cu at (205.4, 91.6)
- added D98: LED_45deg, pcie:LED_WS2812B-2020_PLCC4_2.0x2.0mm, B.Cu at (210.1, 91.6)
- added D99: LED_45deg, pcie:LED_WS2812B-2020_PLCC4_2.0x2.0mm, B.Cu at (214.9, 91.6)
- added H1: MountingHole, MountingHole:MountingHole_3.2mm_M3_Pad, F.Cu at (72.0, 99.4)
- added H2: MountingHole, MountingHole:MountingHole_3.2mm_M3_Pad, F.Cu at (72.0, 184.8)
- added J12: Conn_02x03_Odd_Even, Connector_Molex:Molex_Mini-Fit_Jr_5569-06A1_2x03_P4.20mm_Horizontal, F.Cu at (220.3, 106.9)
- added J13: 12V, Connector_PinHeader_2.54mm:PinHeader_1x01_P2.54mm_Vertical, F.Cu at (222.6, 157.1)
- added J14: 5V, Connector_PinHeader_2.54mm:PinHeader_1x01_P2.54mm_Vertical, F.Cu at (222.6, 163.1)
- added J15: 5V, Connector_PinHeader_2.54mm:PinHeader_1x01_P2.54mm_Vertical, F.Cu at (222.6, 160.1)
- added L5: 33uH, Inductor_SMD:L_APV_APH1050, F.Cu at (222.6, 128.6)
- added L6: 33uH, Inductor_SMD:L_APV_APH1050, B.Cu at (212.6, 128.6)
- added R50: 1k, Resistor_SMD:R_0402_1005Metric, F.Cu at (95.7, 175.1)
- added R51: 270, Resistor_SMD:R_0402_1005Metric, F.Cu at (92.7, 175.1)
- added R52: 100, Resistor_SMD:R_0402_1005Metric, F.Cu at (89.7, 175.1)
- added R53: 3k, Resistor_SMD:R_0402_1005Metric, F.Cu at (211.1, 138.1)
- added R54: 1k, Resistor_SMD:R_0402_1005Metric, F.Cu at (209.1, 139.4)
- added R55: 3k, Resistor_SMD:R_0402_1005Metric, B.Cu at (224.1, 138.1)
- added R56: 1k, Resistor_SMD:R_0402_1005Metric, B.Cu at (226.1, 139.4)
- added R57: 1k, Resistor_SMD:R_0402_1005Metric, F.Cu at (225.1, 156.6)
- added R58: 1k, Resistor_SMD:R_0402_1005Metric, F.Cu at (225.1, 157.6)
- added R59: 270, Resistor_SMD:R_0402_1005Metric, F.Cu at (225.1, 162.6)
- added R60: 270, Resistor_SMD:R_0402_1005Metric, F.Cu at (225.1, 163.6)
- added R61: 270, Resistor_SMD:R_0402_1005Metric, F.Cu at (225.1, 159.6)
- added R62: 270, Resistor_SMD:R_0402_1005Metric, F.Cu at (225.1, 160.6)
- added U10: XL4015, Package_TO_SOT_SMD:TO-263-5_TabPin3, B.Cu at (212.6, 140.1)
- added U9: XL4015, Package_TO_SOT_SMD:TO-263-5_TabPin3, F.Cu at (222.6, 140.1)
- C10, C11, C14, C15, C18, C3, C34, C36, C38, C40, C5, C7: value 1u -> 1uF
- C12, C13, C16, C17, C33, C35, C39, C4, C41, C54, C55, C56, C57, C58, C59, C6, C60, C61, C62, C63, C64, C8, C9: value 100n -> 100nF
- C42, C46, C50, C51, C52: value 10u -> 10uF
- C43, C44, C45, C47, C48, C49, C53: value 22u -> 22uF
- R3: value R -> 1k
- R4: value R -> 270
- R5: value R -> 100
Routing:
- net LED_5V2: track 0.00 -> 283.4 mm, vias 0 -> 71
- net LED_5V1: track 0.00 -> 268.5 mm, vias 0 -> 72
- net Net-(D200-K): track 0.00 -> 9.15 mm
- net Net-(D199-K): track 0.00 -> 9.15 mm
- net +12VE: track 0.00 -> 7.99 mm, vias 0 -> 8
- net Net-(U9-FB): track 0.00 -> 7.42 mm
- net Net-(U10-FB): track 0.00 -> 7.42 mm
- net Net-(D38-DOUT): track 0.00 -> 4.44 mm
- net Net-(D70-DOUT): track 0.00 -> 4.26 mm
- net Net-(D134-DOUT): track 0.00 -> 4.26 mm
- net Net-(D166-DOUT): track 0.00 -> 3.97 mm
- net Net-(D102-DOUT): track 0.00 -> 3.93 mm
- net Net-(U9-VC): track 0.00 -> 3.61 mm
- net Net-(U10-VC): track 0.00 -> 3.61 mm
- net Net-(D98-DOUT): track 0.00 -> 3.38 mm, vias 0 -> 2
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- added copper zone on B.Cu, net +12VE
- added copper zone on F.Cu, net +12VE
- added copper zone on In2.Cu, net +12VE
- added copper zone on In1.Cu, net GND
- added copper zone on B.Cu, net LED_5V1
- added copper zone on In1.Cu, net LED_5V1
- added copper zone on In2.Cu, net LED_5V1
- added copper zone on F.Cu, net LED_5V2
- added copper zone on In1.Cu, net LED_5V2
- added copper zone on In2.Cu, net LED_5V2
- added copper zone on F.Cu, net Net-(D199-K)
- added copper zone on B.Cu, net Net-(D200-K)
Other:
- board size 167.7 x 111.2 mm -> 167.6 x 111.2 mm
- board text added: "12VE"
- board text added: "5V1"
- board text added: "5V2"
- board text added: "powaaaaa"
